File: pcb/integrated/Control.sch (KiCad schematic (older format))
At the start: 0 parts

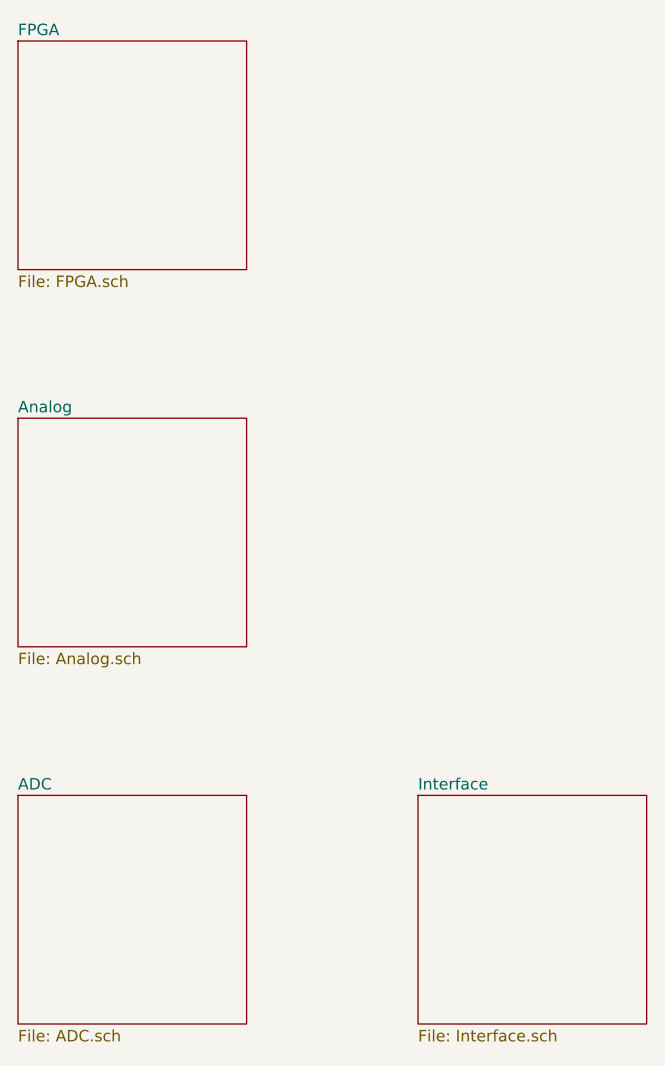
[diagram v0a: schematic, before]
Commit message: schematic fixes and component placement
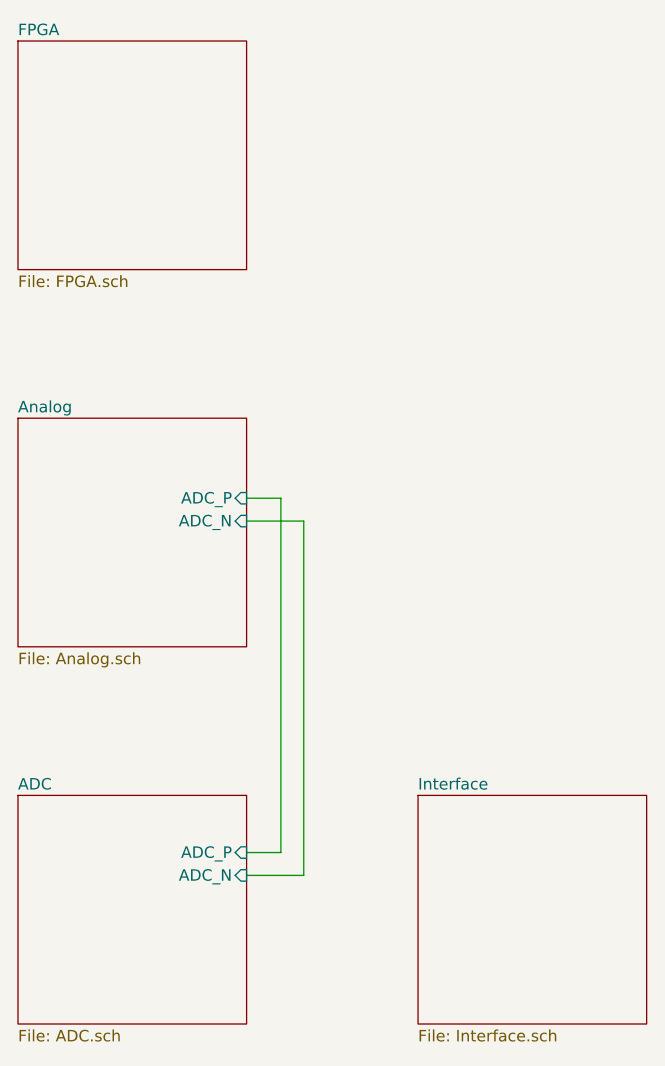
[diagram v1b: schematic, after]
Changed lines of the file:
@@
 F0 "Analog" 50
 F1 "Analog.sch" 50
+F2 "ADC_P" I R 2000 3350 50
+F3 "ADC_N" I R 2000 3450 50
 $EndSheet
 $Sheet
@@
 F0 "ADC" 50
 F1 "ADC.sch" 50
+F2 "ADC_P" I R 2000 4900 50
+F3 "ADC_N" I R 2000 5000 50
 $EndSheet
 $Sheet
@@
 F1 "Interface.sch" 50
 $EndSheet
+Wire Wire Line
+	2000 3350 2150 3350
+Wire Wire Line
+	2150 3350 2150 4900
+Wire Wire Line
+	2150 4900 2000 4900
+Wire Wire Line
+	2000 3450 2250 3450
+Wire Wire Line
+	2250 3450 2250 5000
+Wire Wire Line
+	2250 5000 2000 5000
 $EndSCHEMATC
